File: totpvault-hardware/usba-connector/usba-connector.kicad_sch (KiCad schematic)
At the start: 27 parts, among them J3 Conn_01x06_Socket, U1 ESP32-C3, U2 HT75xx-1-SOT89, U3 CH343P, U4 USBLC6-2SC6, Y1 Crystal_GND24

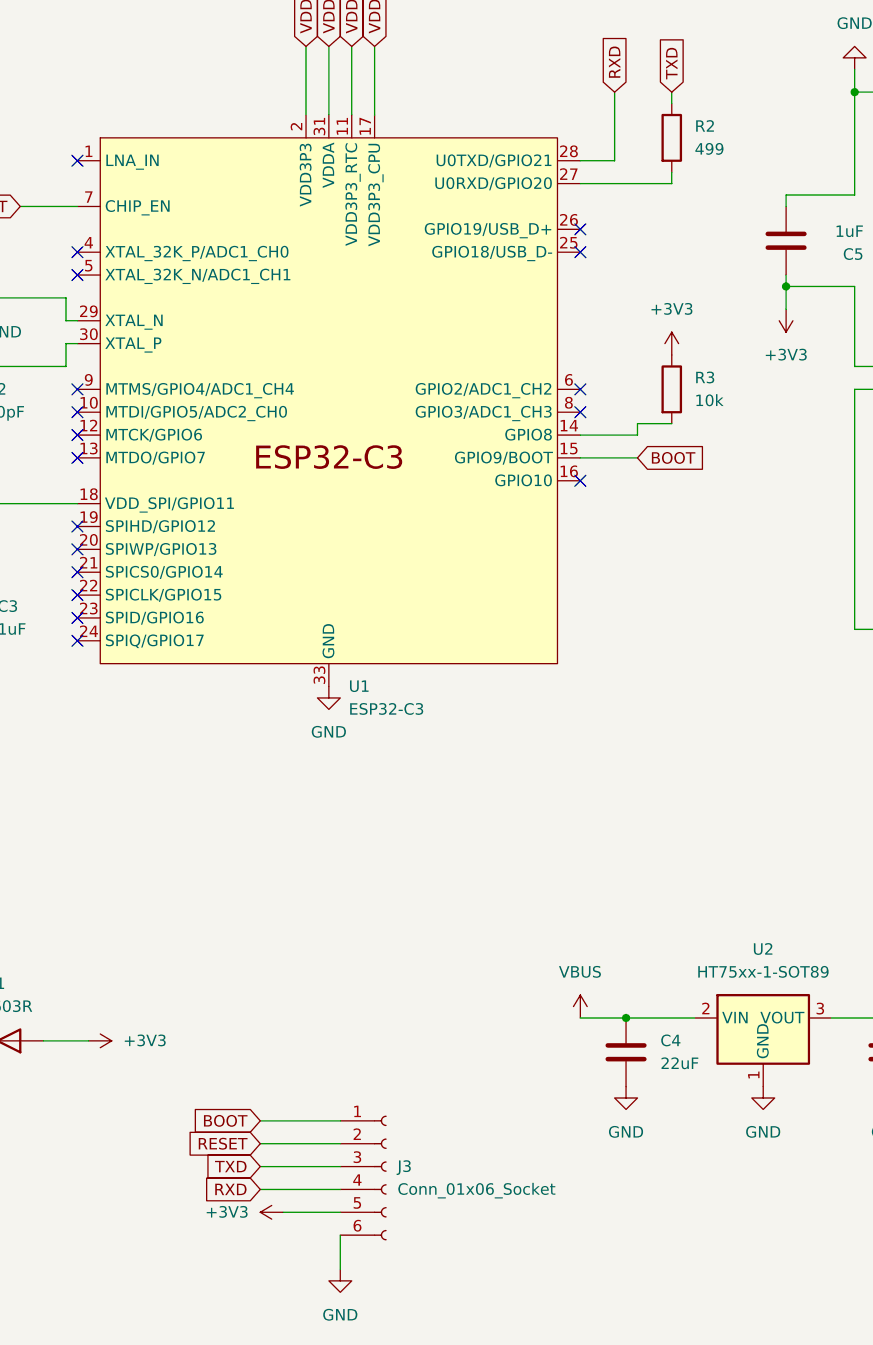
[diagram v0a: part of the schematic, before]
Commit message: Finalized USB-A PCB
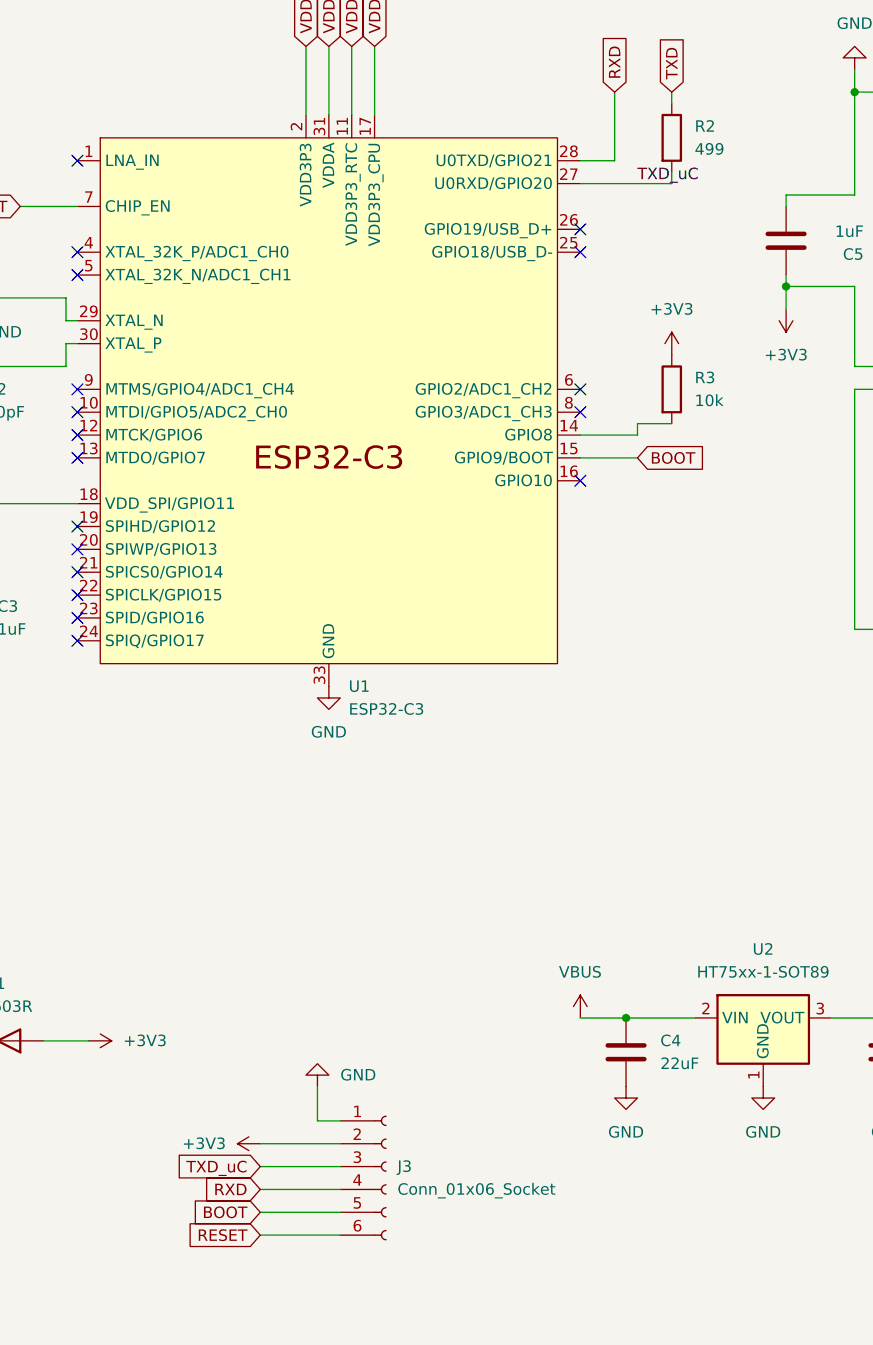
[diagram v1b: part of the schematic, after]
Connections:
- net +3V3: now also J3.2 (Pin_2); no longer J3.5 (Pin_5)
- net BOOT: now also J3.5 (Pin_5); no longer J3.1 (Pin_1)
- net GND: now also J3.1 (Pin_1); no longer J3.6 (Pin_6)
- net RESET: now also J3.6 (Pin_6); no longer J3.2 (Pin_2)
- net TXD: no longer J3.3 (Pin_3)
- net TXD_uC: now reaches R2.2, U1.27 (U0RXD/GPIO20)
- net TXD_uC: now also J3.3 (Pin_3)
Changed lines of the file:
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@@
 	(wire
 		(pts
+			(xy 80.01 173.99) (xy 88.9 173.99)
+		)
+		(stroke
+			(width 0)
+			(type default)
+		)
+	)
+	(wire
+		(pts
 			(xy 143.51 160.02) (xy 149.86 160.02)
 		)
@@
 	(wire
 		(pts
+			(xy 86.36 167.64) (xy 86.36 171.45)
+		)
+		(stroke
+			(width 0)
+			(type default)
+		)
+	)
+	(wire
+		(pts
 			(xy 146.05 78.74) (xy 138.43 78.74)
 		)
@@
 	(wire
 		(pts
+			(xy 86.36 171.45) (xy 88.9 171.45)
+		)
+		(stroke
+			(width 0)
+			(type default)
+		)
+	)
+	(wire
+		(pts
 			(xy 236.22 85.09) (xy 236.22 100.33)
 		)
@@
 	(wire
 		(pts
-			(xy 115.57 160.02) (xy 120.65 160.02)
+			(xy 80.01 181.61) (xy 88.9 181.61)
 		)
 		(stroke
@@
 	(wire
 		(pts
-			(xy 80.01 173.99) (xy 88.9 173.99)
+			(xy 115.57 160.02) (xy 120.65 160.02)
 		)
 		(stroke
@@
 	(wire
 		(pts
-			(xy 82.55 181.61) (xy 88.9 181.61)
-		)
-		(stroke
-			(width 0)
-			(type default)
-		)
-	)
-	(wire
-		(pts
 			(xy 203.2 139.7) (xy 214.63 139.7)
 		)
@@
 	(wire
 		(pts
-			(xy 88.9 184.15) (xy 88.9 187.96)
-		)
-		(stroke
-			(width 0)
-			(type default)
-		)
-	)
-	(wire
-		(pts
 			(xy 146.05 116.84) (xy 170.18 116.84)
 		)
@@
 	(wire
 		(pts
-			(xy 80.01 171.45) (xy 88.9 171.45)
-		)
-		(stroke
-			(width 0)
-			(type default)
-		)
-	)
-	(wire
-		(pts
 			(xy 262.89 110.49) (xy 267.97 110.49)
 		)
@@
 	(wire
 		(pts
+			(xy 80.01 184.15) (xy 88.9 184.15)
+		)
+		(stroke
+			(width 0)
+			(type default)
+		)
+	)
+	(wire
+		(pts
 			(xy 243.84 77.47) (xy 227.33 77.47)
 		)
@@
 		)
 	)
+	(label "TXD_uC"
+		(at 121.92 67.31 0)
+		(effects
+			(font
+				(size 1.27 1.27)
+			)
+			(justify left bottom)
+		)
+	)
 	(label "EMI_D-"
 		(at 195.58 62.23 0)
@@
 	(global_label "BOOT"
 		(shape input)
-		(at 80.01 171.45 180)
+		(at 80.01 181.61 180)
 		(fields_autoplaced yes)
 		(effects
@@
 		)
 		(property "Intersheetrefs" "${INTERSHEET_REFS}"
-			(at 72.1262 171.45 0)
+			(at 72.1262 181.61 0)
 			(effects
 				(font
@@
 	(global_label "RESET"
 		(shape input)
-		(at 80.01 173.99 180)
+		(at 80.01 184.15 180)
 		(fields_autoplaced yes)
 		(effects
@@
 		)
 		(property "Intersheetrefs" "${INTERSHEET_REFS}"
-			(at 71.2797 173.99 0)
+			(at 71.2797 184.15 0)
 			(effects
 				(font
@@
 		)
 	)
-	(global_label "TXD"
+	(global_label "TXD_uC"
 		(shape input)
 		(at 80.01 176.53 180)
@@
 		)
 		(property "Intersheetrefs" "${INTERSHEET_REFS}"
-			(at 73.5777 176.53 0)
+			(at 70.1911 176.53 0)
 			(effects
 				(font
@@
 	(symbol
 		(lib_id "power:+3V3")
-		(at 82.55 181.61 90)
+		(at 80.01 173.99 90)
 		(unit 1)
 		(exclude_from_sim no)
@@
 		(fields_autoplaced yes)
 		(property "Reference" "#PWR08"
-			(at 86.36 181.61 0)
+			(at 83.82 173.99 0)
 			(effects
 				(font
@@
 		)
 		(property "Value" "+3V3"
-			(at 78.74 181.6099 90)
+			(at 76.2 173.9899 90)
 			(effects
 				(font
@@
 		)
 		(property "Footprint" ""
-			(at 82.55 181.61 0)
+			(at 80.01 173.99 0)
 			(effects
 				(font
@@
 		)
 		(property "Datasheet" ""
-			(at 82.55 181.61 0)
+			(at 80.01 173.99 0)
 			(effects
 				(font
@@
 		)
 		(property "Description" "Power symbol creates a global label with name \"+3V3\""
-			(at 82.55 181.61 0)
+			(at 80.01 173.99 0)
 			(effects
 				(font
@@
 	(symbol
 		(lib_id "power:GND")
-		(at 88.9 187.96 0)
+		(at 86.36 167.64 180)
 		(unit 1)
 		(exclude_from_sim no)
@@
 		(fields_autoplaced yes)
 		(property "Reference" "#PWR010"
-			(at 88.9 194.31 0)
+			(at 86.36 161.29 0)
 			(effects
 				(font
@@
 		)
 		(property "Value" "GND"
-			(at 88.9 193.04 0)
+			(at 88.9 166.3699 0)
 			(effects
 				(font
 					(size 1.27 1.27)
 				)
+				(justify right)
 			)
 		)
 		(property "Footprint" ""
-			(at 88.9 187.96 0)
+			(at 86.36 167.64 0)
 			(effects
 				(font
@@
 		)
 		(property "Datasheet" ""
-			(at 88.9 187.96 0)
+			(at 86.36 167.64 0)
 			(effects
 				(font
@@
 		)
 		(property "Description" "Power symbol creates a global label with name \"GND\" , ground"
-			(at 88.9 187.96 0)
+			(at 86.36 167.64 0)
 			(effects
 				(font

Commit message: Order ready for USB-A
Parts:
- added TP1, TP2, TP3: TestPoint_Probe, TestPoint:TestPoint_Pad_D1.0mm, symbol Connector:TestPoint_Probe
- C4, C6: value 22uF -> 10uF
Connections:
- net +3V3: now also TP3.1
- net GND: now also TP2.1
- net VBUS: now also TP1.1

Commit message: Modified USB-A connector to use a physical connector instead of PCB slice due to pricing of ordering 2mm gold-plated PCBs
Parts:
- X1: footprint Custom:usb-PCB -> Connector_USB:USB_A_Molex_48037-2200_Horizontal
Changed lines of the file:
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@@
 			)
 		)
-		(property "Footprint" "Custom:usb-PCB"
+		(property "Footprint" "Connector_USB:USB_A_Molex_48037-2200_Horizontal"
 			(at 237.49 68.58 0)
 			(effects

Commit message: PCB Order
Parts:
- removed R2: 499, Resistor_SMD:R_0402_1005Metric, symbol Device:R
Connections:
- net TXD_uC is gone; now on net TXD: J3.3 (Pin_3), U1.27 (U0RXD/GPIO20)
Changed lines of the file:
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@@
 	(wire
 		(pts
+			(xy 125.73 57.15) (xy 125.73 67.31)
+		)
+		(stroke
+			(width 0)
+			(type default)
+		)
+	)
+	(wire
+		(pts
 			(xy 214.63 139.7) (xy 222.25 139.7)
 		)
@@
 	(wire
 		(pts
-			(xy 125.73 67.31) (xy 125.73 66.04)
-		)
-		(stroke
-			(width 0)
-			(type default)
-		)
-	)
-	(wire
-		(pts
 			(xy 267.97 110.49) (xy 274.32 110.49)
 		)
@@
 	(wire
 		(pts
-			(xy 125.73 58.42) (xy 125.73 57.15)
-		)
-		(stroke
-			(width 0)
-			(type default)
-		)
-	)
-	(wire
-		(pts
 			(xy 170.18 116.84) (xy 196.85 116.84)
 		)
@@
 		)
 	)
-	(label "TXD_uC"
-		(at 121.92 67.31 0)
-		(effects
-			(font
-				(size 1.27 1.27)
-			)
-			(justify left bottom)
-		)
-	)
 	(label "EMI_D-"
 		(at 195.58 62.23 0)
@@
 		)
 	)
-	(global_label "TXD_uC"
+	(global_label "TXD"
 		(shape input)
 		(at 80.01 176.53 180)
@@
 		)
 		(property "Intersheetrefs" "${INTERSHEET_REFS}"
-			(at 70.1911 176.53 0)
+			(at 73.5777 176.53 0)
 			(effects
 				(font
@@
 					(unit 1)
 				)
-			)
-		)
-	)
-	(symbol
-		(lib_id "Device:R")
-		(at 125.73 62.23 0)
-		(unit 1)
-		(exclude_from_sim no)
-		(in_bom yes)
-		(on_board yes)
-		(dnp no)
-		(fields_autoplaced yes)
-		(property "Reference" "R2"
-			(at 128.27 60.9599 0)
-			(effects
-				(font
-					(size 1.27 1.27)
-				)
-				(justify left)
-			)
-		)
-		(property "Value" "499"
-			(at 128.27 63.4999 0)
-			(effects
-				(font
-					(size 1.27 1.27)
-				)
-				(justify left)
-			)
-		)
-		(property "Footprint" "Resistor_SMD:R_0402_1005Metric"
-			(at 123.952 62.23 90)
-			(effects
-				(font
-					(size 1.27 1.27)
-				)
-				(hide yes)
-			)
-		)
-		(property "Datasheet" "~"
-			(at 125.73 62.23 0)
-			(effects
-				(font
-					(size 1.27 1.27)
-				)
-				(hide yes)
-			)
-		)
-		(property "Description" "Resistor"
-			(at 125.73 62.23 0)
-			(effects
-				(font
-					(size 1.27 1.27)
-				)
-				(hide yes)
-			)
-		)
-		(pin "2"
-		)
-		(pin "1"
-		)
-		(instances
-			(project "usba-connector"
-				(path "/0954aedb-d4b2-4b60-84d2-99d5716b5943"
-					(reference "R2")
-					(unit 1)
-				)
